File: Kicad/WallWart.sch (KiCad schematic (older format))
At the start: 7 parts, among them CON1 LB_BarrelJack, P2 V+_WallWart, U5 LM7805

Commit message: Layout with traces - ran through ERC and DRC
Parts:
- removed U5: LM7805, ~, symbol MCP1703
- added U3: MC78L05, ~, symbol MC78L05
- P2: value V+_WallWart -> WallWartExtension
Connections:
- net labels removed: Vin
- wire segments 15 -> 17
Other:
- moved on the sheet: P2
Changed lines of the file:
@@
 Sheet 4 7
 Title ""
-Date "14 aug 2014"
+Date "19 aug 2014"
 Rev ""
 Comp ""
@@
 Comment4 ""
 $EndDescr
-$Comp
-L MCP1703 U5
-U 1 1 53DB8BFE
-P 5600 3650
-F 0 "U5" H 5750 3650 60  0000 C CNN
-F 1 "LM7805" H 5600 4100 60  0000 C CNN
-F 2 "~" H 5600 3650 60  0000 C CNN
-F 3 "~" H 5600 3650 60  0000 C CNN
-	1    5600 3650
-	1    0    0    -1
-$EndComp
 $Comp
 L C C12
@@
 $EndComp
 Wire Wire Line
-	6250 3450 7950 3450
-Wire Wire Line
-	7200 3450 7200 3550
-Wire Wire Line
-	6800 3550 6800 3450
-Connection ~ 6800 3450
-Wire Wire Line
-	5600 3900 5600 4100
+	5600 3750 5600 4100
 Wire Wire Line
 	3750 4100 7200 4100
@@
 	6800 3950 6800 4100
 Connection ~ 6800 4100
-Wire Wire Line
-	4350 3450 5000 3450
-Wire Wire Line
-	4750 3450 4750 3550
 Wire Wire Line
 	4750 4100 4750 3950
@@
 Wire Wire Line
 	3950 3450 3750 3450
-Connection ~ 4750 3450
 Wire Wire Line
 	3750 3550 3750 4100
 Connection ~ 4750 4100
 Connection ~ 3750 3650
-Connection ~ 7200 3450
 Text Notes 3150 3150 0    60   ~ 0
 6.25V - 12V
@@
 V+_WallWart
 $Comp
-L AGND #PWR10
+L AGND #PWR010
 U 1 1 53DCDB22
 P 5250 4450
-F 0 "#PWR10" H 5250 4450 40  0001 C CNN
+F 0 "#PWR010" H 5250 4450 40  0001 C CNN
 F 1 "AGND" H 5250 4380 50  0000 C CNN
 F 2 "" H 5250 4450 60  0000 C CNN
@@
 	5250 4450 5250 4100
 Connection ~ 5250 4100
-Text Label 4850 3450 0    60   ~ 0
-Vin
-Text Label 3850 3450 0    60   ~ 0
-Vin
 $Comp
 L CONN_2 P2
 U 1 1 53E89338
-P 7500 2900
-F 0 "P2" V 7450 2900 40  0000 C CNN
-F 1 "V+_WallWart" V 7550 2900 40  0000 C CNN
-F 2 "" H 7500 2900 60  0000 C CNN
-F 3 "" H 7500 2900 60  0000 C CNN
-	1    7500 2900
+P 7500 2450
+F 0 "P2" V 7450 2450 40  0000 C CNN
+F 1 "WallWartExtension" V 7550 2450 40  0000 C CNN
+F 2 "" H 7500 2450 60  0000 C CNN
+F 3 "" H 7500 2450 60  0000 C CNN
+	1    7500 2450
 	0    -1   -1   0
 $EndComp
 Wire Wire Line
-	7400 3250 7400 3450
-Connection ~ 7400 3450
+	7600 2800 7600 3450
+$Comp
+L AGND #PWR011
+U 1 1 53F2345C
+P 7400 2950
+F 0 "#PWR011" H 7400 2950 40  0001 C CNN
+F 1 "AGND" H 7400 2880 50  0000 C CNN
+F 2 "" H 7400 2950 60  0000 C CNN
+F 3 "" H 7400 2950 60  0000 C CNN
+	1    7400 2950
+	1    0    0    -1
+$EndComp
 Wire Wire Line
-	7600 3250 7600 3450
-Connection ~ 7600 3450
+	7400 2800 7400 2950
+$Comp
+L MC78L05 U3
+U 1 1 53F37E5C
+P 5600 3500
+F 0 "U3" H 5750 3500 60  0000 C CNN
+F 1 "MC78L05" H 5600 3950 60  0000 C CNN
+F 2 "~" H 5600 3500 60  0000 C CNN
+F 3 "~" H 5600 3500 60  0000 C CNN
+	1    5600 3500
+	1    0    0    -1
+$EndComp
+Wire Wire Line
+	6250 3300 7200 3300
+Wire Wire Line
+	7200 3300 7200 3550
+Wire Wire Line
+	6800 3550 6800 3300
+Connection ~ 6800 3300
+Wire Wire Line
+	4350 3450 4450 3450
+Wire Wire Line
+	4450 3450 4450 3300
+Wire Wire Line
+	4450 3300 5000 3300
+Wire Wire Line
+	4750 3550 4750 3300
+Connection ~ 4750 3300
 $EndSCHEMATC

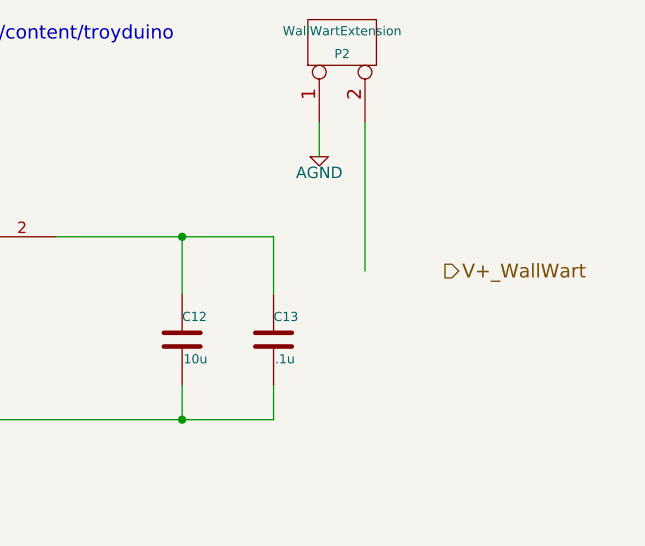
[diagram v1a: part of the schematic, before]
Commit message: updates to layout based on DRC/DFM checks
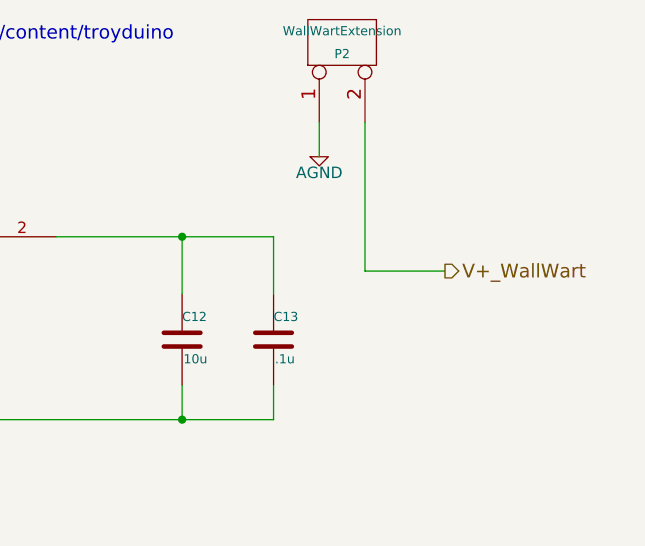
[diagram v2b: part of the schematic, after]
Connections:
- wire segments 17 -> 18
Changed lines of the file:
@@
 Sheet 4 7
 Title ""
-Date "19 aug 2014"
+Date "20 aug 2014"
 Rev ""
 Comp ""
@@
 	4750 3550 4750 3300
 Connection ~ 4750 3300
+Wire Wire Line
+	7600 3450 7950 3450
 $EndSCHEMATC

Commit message: Dev Rev 1
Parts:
- added D3: 4004, ~, symbol DIODE
- added TP10, TP11, TP9: CONN_1, symbol CONN_1
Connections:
- net AGND: now also TP10.1
- net V+_WallWart: now also D3.2 (K), TP11.1; no longer P2.2 (PM)
- net at C12.1, C13.1, U3.2: now also P2.2 (PM), D3.1 (A)
- net at C11.1, D2.2 (K), U3.3: now also TP9.1
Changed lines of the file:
@@
 Sheet 4 7
 Title ""
-Date "20 aug 2014"
+Date "21 aug 2014"
 Rev ""
 Comp ""
@@
 Text Notes 4700 2450 0    60   ~ 0
 see http://www.troydowling.org/content/troyduino
-Text HLabel 7950 3450 2    60   Output ~ 0
+Text HLabel 9150 3450 2    60   Output ~ 0
 V+_WallWart
 $Comp
@@
 $EndComp
 Wire Wire Line
-	6250 3300 7200 3300
+	6250 3300 7600 3300
 Wire Wire Line
 	7200 3300 7200 3550
@@
 Connection ~ 6800 3300
 Wire Wire Line
-	4350 3450 4450 3450
-Wire Wire Line
-	4450 3450 4450 3300
+	4450 3450 4350 3450
+Wire Wire Line
+	4450 3050 4450 3450
 Wire Wire Line
 	4450 3300 5000 3300
@@
 Connection ~ 4750 3300
 Wire Wire Line
-	7600 3450 7950 3450
+	7600 3450 8350 3450
+Connection ~ 7200 3300
+Connection ~ 7600 3300
+$Comp
+L DIODE D3
+U 1 1 53F5B6B0
+P 8550 3450
+F 0 "D3" H 8550 3550 40  0000 C CNN
+F 1 "4004" H 8550 3350 40  0000 C CNN
+F 2 "~" H 8550 3450 60  0000 C CNN
+F 3 "~" H 8550 3450 60  0000 C CNN
+	1    8550 3450
+	1    0    0    -1
+$EndComp
+Wire Wire Line
+	8750 3450 9150 3450
+$Comp
+L CONN_1 TP9
+U 1 1 53F5FBA0
+P 4600 3050
+F 0 "TP9" H 4680 3050 40  0000 L CNN
+F 1 "CONN_1" H 4600 3105 30  0001 C CNN
+F 2 "" H 4600 3050 60  0000 C CNN
+F 3 "" H 4600 3050 60  0000 C CNN
+	1    4600 3050
+	1    0    0    -1
+$EndComp
+Connection ~ 4450 3300
+$Comp
+L CONN_1 TP11
+U 1 1 53F5FBD1
+P 9100 3000
+F 0 "TP11" H 9180 3000 40  0000 L CNN
+F 1 "CONN_1" H 9100 3055 30  0001 C CNN
+F 2 "" H 9100 3000 60  0000 C CNN
+F 3 "" H 9100 3000 60  0000 C CNN
+	1    9100 3000
+	1    0    0    -1
+$EndComp
+Wire Wire Line
+	8950 3000 8950 3450
+Connection ~ 8950 3450
+$Comp
+L CONN_1 TP10
+U 1 1 53F5FBF5
+P 6250 3850
+F 0 "TP10" H 6330 3850 40  0000 L CNN
+F 1 "CONN_1" H 6250 3905 30  0001 C CNN
+F 2 "" H 6250 3850 60  0000 C CNN
+F 3 "" H 6250 3850 60  0000 C CNN
+	1    6250 3850
+	1    0    0    -1
+$EndComp
+Wire Wire Line
+	6100 3850 6100 4100
+Connection ~ 6100 4100
 $EndSCHEMATC

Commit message: updates for dev rev 2
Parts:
- removed TP11: CONN_1, symbol CONN_1
- added D?: LED, ~, symbol LED
- added R?: 120, ~, symbol R
- added TP?: CONN_1, symbol CONN_1
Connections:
- net V+_WallWart: now also D?.2 (K), TP?.1; no longer D3.2 (K)
- net at C12.1, C13.1, D3.1 (A)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: no longer P2.2 (PM)
- new net: D3.2 (K), P2.2 (PM), R?.1
- new net: D?.1 (A), R?.2
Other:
- moved on the sheet: D3, P2
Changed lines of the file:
@@
 Sheet 4 7
 Title ""
-Date "21 aug 2014"
+Date "9 sep 2014"
 Rev ""
 Comp ""
@@
 $EndComp
 Wire Wire Line
-	5600 3750 5600 4100
+	5600 4100 5600 3750
 Wire Wire Line
 	3750 4100 7200 4100
@@
 Text Notes 4700 2450 0    60   ~ 0
 see http://www.troydowling.org/content/troyduino
-Text HLabel 9150 3450 2    60   Output ~ 0
+Text HLabel 10050 3300 2    60   Output ~ 0
 V+_WallWart
 $Comp
@@
 L CONN_2 P2
 U 1 1 53E89338
-P 7500 2450
-F 0 "P2" V 7450 2450 40  0000 C CNN
-F 1 "WallWartExtension" V 7550 2450 40  0000 C CNN
-F 2 "" H 7500 2450 60  0000 C CNN
-F 3 "" H 7500 2450 60  0000 C CNN
-	1    7500 2450
+P 8250 2450
+F 0 "P2" V 8200 2450 40  0000 C CNN
+F 1 "WallWartExtension" V 8300 2450 40  0000 C CNN
+F 2 "" H 8250 2450 60  0000 C CNN
+F 3 "" H 8250 2450 60  0000 C CNN
+	1    8250 2450
 	0    -1   -1   0
 $EndComp
 Wire Wire Line
-	7600 2800 7600 3450
+	8350 2800 8350 3300
 $Comp
 L AGND #PWR011
 U 1 1 53F2345C
-P 7400 2950
-F 0 "#PWR011" H 7400 2950 40  0001 C CNN
-F 1 "AGND" H 7400 2880 50  0000 C CNN
-F 2 "" H 7400 2950 60  0000 C CNN
-F 3 "" H 7400 2950 60  0000 C CNN
-	1    7400 2950
-	1    0    0    -1
-$EndComp
-Wire Wire Line
-	7400 2800 7400 2950
+P 8150 2950
+F 0 "#PWR011" H 8150 2950 40  0001 C CNN
+F 1 "AGND" H 8150 2880 50  0000 C CNN
+F 2 "" H 8150 2950 60  0000 C CNN
+F 3 "" H 8150 2950 60  0000 C CNN
+	1    8150 2950
+	1    0    0    -1
+$EndComp
+Wire Wire Line
+	8150 2800 8150 2950
 $Comp
 L MC78L05 U3
@@
 $EndComp
 Wire Wire Line
-	6250 3300 7600 3300
-Wire Wire Line
-	7200 3300 7200 3550
-Wire Wire Line
-	6800 3550 6800 3300
+	6250 3300 7400 3300
+Wire Wire Line
+	6800 3300 6800 3550
 Connection ~ 6800 3300
 Wire Wire Line
@@
 	4750 3550 4750 3300
 Connection ~ 4750 3300
-Wire Wire Line
-	7600 3450 8350 3450
-Connection ~ 7200 3300
-Connection ~ 7600 3300
+Connection ~ 8350 3300
 $Comp
 L DIODE D3
 U 1 1 53F5B6B0
-P 8550 3450
-F 0 "D3" H 8550 3550 40  0000 C CNN
-F 1 "4004" H 8550 3350 40  0000 C CNN
-F 2 "~" H 8550 3450 60  0000 C CNN
-F 3 "~" H 8550 3450 60  0000 C CNN
-	1    8550 3450
-	1    0    0    -1
-$EndComp
-Wire Wire Line
-	8750 3450 9150 3450
+P 7600 3300
+F 0 "D3" H 7600 3400 40  0000 C CNN
+F 1 "4004" H 7600 3200 40  0000 C CNN
+F 2 "~" H 7600 3300 60  0000 C CNN
+F 3 "~" H 7600 3300 60  0000 C CNN
+	1    7600 3300
+	1    0    0    -1
+$EndComp
 $Comp
 L CONN_1 TP9
@@
 Connection ~ 4450 3300
 $Comp
-L CONN_1 TP11
-U 1 1 53F5FBD1
-P 9100 3000
-F 0 "TP11" H 9180 3000 40  0000 L CNN
-F 1 "CONN_1" H 9100 3055 30  0001 C CNN
-F 2 "" H 9100 3000 60  0000 C CNN
-F 3 "" H 9100 3000 60  0000 C CNN
-	1    9100 3000
-	1    0    0    -1
-$EndComp
-Wire Wire Line
-	8950 3000 8950 3450
-Connection ~ 8950 3450
-$Comp
 L CONN_1 TP10
 U 1 1 53F5FBF5
@@
 	6100 3850 6100 4100
 Connection ~ 6100 4100
+$Comp
+L LED D?
+U 1 1 540ED65C
+P 9400 3300
+F 0 "D?" H 9400 3400 50  0000 C CNN
+F 1 "LED" H 9400 3200 50  0000 C CNN
+F 2 "~" H 9400 3300 60  0000 C CNN
+F 3 "~" H 9400 3300 60  0000 C CNN
+	1    9400 3300
+	1    0    0    -1
+$EndComp
+Text Label 8100 3700 0    60   ~ 0
+Green Status LED always on when there is power
+$Comp
+L R R?
+U 1 1 540EDC27
+P 8750 3300
+F 0 "R?" V 8830 3300 40  0000 C CNN
+F 1 "120" V 8757 3301 40  0000 C CNN
+F 2 "~" V 8680 3300 30  0000 C CNN
+F 3 "~" H 8750 3300 30  0000 C CNN
+	1    8750 3300
+	0    -1   -1   0
+$EndComp
+Wire Wire Line
+	7800 3300 8500 3300
+Wire Wire Line
+	9000 3300 9200 3300
+Wire Wire Line
+	9600 3300 10050 3300
+Wire Wire Line
+	7200 3300 7200 3550
+Connection ~ 7200 3300
+Text Label 7050 1600 0    60   ~ 0
+http://media.digikey.com/pdf/Data%20Sheets/Lite-On%20PDFs/LTST-C171GKT.pdf
+Text Label 8600 1300 0    60   ~ 0
+LED: 20mA, 2.5 forward voltage
+$Comp
+L CONN_1 TP?
+U 1 1 540EE2E1
+P 9950 2950
+F 0 "TP?" H 10030 2950 40  0000 L CNN
+F 1 "CONN_1" H 9950 3005 30  0001 C CNN
+F 2 "" H 9950 2950 60  0000 C CNN
+F 3 "" H 9950 2950 60  0000 C CNN
+	1    9950 2950
+	1    0    0    -1
+$EndComp
+Wire Wire Line
+	9800 2950 9800 3300
+Connection ~ 9800 3300
 $EndSCHEMATC

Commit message: Ready for Schematic Design Review
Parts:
- removed D3: 4004, ~, symbol DIODE
- R5: renamed from R?; value 120 -> 1K
- gave numbers to parts that had none: 2
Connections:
- net AGND: now also R5.1
- net V+_WallWart: now also C12.1, C13.1, D3.1 (A), P2.2 (PM), U3.2; no longer D3.2 (K)
- net at R5.2: now also D3.2 (K); no longer D3.1 (A)
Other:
- note removed: "see http://www.troydowling.org/content/troyduino"
- moved on the sheet: D3, R5
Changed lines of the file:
@@
 $Descr A4 11693 8268
 encoding utf-8
-Sheet 4 7
+Sheet 2 7
 Title ""
-Date "9 sep 2014"
+Date "10 sep 2014"
 Rev ""
 Comp ""
@@
 Text Notes 3150 3150 0    60   ~ 0
 6.25V - 12V
-Text Notes 4700 2450 0    60   ~ 0
-see http://www.troydowling.org/content/troyduino
 Text HLabel 10050 3300 2    60   Output ~ 0
 V+_WallWart
 $Comp
-L AGND #PWR010
+L AGND #PWR01
 U 1 1 53DCDB22
 P 5250 4450
-F 0 "#PWR010" H 5250 4450 40  0001 C CNN
+F 0 "#PWR01" H 5250 4450 40  0001 C CNN
 F 1 "AGND" H 5250 4380 50  0000 C CNN
 F 2 "" H 5250 4450 60  0000 C CNN
@@
 $EndComp
 Wire Wire Line
-	8350 2800 8350 3300
-$Comp
-L AGND #PWR011
+	8350 3300 8350 2800
+$Comp
+L AGND #PWR02
 U 1 1 53F2345C
 P 8150 2950
-F 0 "#PWR011" H 8150 2950 40  0001 C CNN
+F 0 "#PWR02" H 8150 2950 40  0001 C CNN
 F 1 "AGND" H 8150 2880 50  0000 C CNN
 F 2 "" H 8150 2950 60  0000 C CNN
@@
 $EndComp
 Wire Wire Line
-	6250 3300 7400 3300
-Wire Wire Line
 	6800 3300 6800 3550
-Connection ~ 6800 3300
 Wire Wire Line
 	4450 3450 4350 3450
@@
 	4750 3550 4750 3300
 Connection ~ 4750 3300
-Connection ~ 8350 3300
-$Comp
-L DIODE D3
-U 1 1 53F5B6B0
-P 7600 3300
-F 0 "D3" H 7600 3400 40  0000 C CNN
-F 1 "4004" H 7600 3200 40  0000 C CNN
-F 2 "~" H 7600 3300 60  0000 C CNN
-F 3 "~" H 7600 3300 60  0000 C CNN
-	1    7600 3300
-	1    0    0    -1
-$EndComp
 $Comp
 L CONN_1 TP9
@@
 Connection ~ 6100 4100
 $Comp
-L LED D?
+L LED D3
 U 1 1 540ED65C
-P 9400 3300
-F 0 "D?" H 9400 3400 50  0000 C CNN
-F 1 "LED" H 9400 3200 50  0000 C CNN
-F 2 "~" H 9400 3300 60  0000 C CNN
-F 3 "~" H 9400 3300 60  0000 C CNN
-	1    9400 3300
-	1    0    0    -1
-$EndComp
-Text Label 8100 3700 0    60   ~ 0
-Green Status LED always on when there is power
-$Comp
-L R R?
+P 8850 3700
+F 0 "D3" H 8850 3800 50  0000 C CNN
+F 1 "LED" H 8850 3600 50  0000 C CNN
+F 2 "~" H 8850 3700 60  0000 C CNN
+F 3 "~" H 8850 3700 60  0000 C CNN
+	1    8850 3700
+	0    1    1    0
+$EndComp
+$Comp
+L R R5
 U 1 1 540EDC27
-P 8750 3300
-F 0 "R?" V 8830 3300 40  0000 C CNN
-F 1 "120" V 8757 3301 40  0000 C CNN
-F 2 "~" V 8680 3300 30  0000 C CNN
-F 3 "~" H 8750 3300 30  0000 C CNN
-	1    8750 3300
-	0    -1   -1   0
-$EndComp
-Wire Wire Line
-	7800 3300 8500 3300
-Wire Wire Line
-	9000 3300 9200 3300
-Wire Wire Line
-	9600 3300 10050 3300
+P 8850 4400
+F 0 "R5" V 8930 4400 40  0000 C CNN
+F 1 "1K" V 8857 4401 40  0000 C CNN
+F 2 "~" V 8780 4400 30  0000 C CNN
+F 3 "~" H 8850 4400 30  0000 C CNN
+	1    8850 4400
+	-1   0    0    1
+$EndComp
+Wire Wire Line
+	6250 3300 10050 3300
 Wire Wire Line
 	7200 3300 7200 3550
-Connection ~ 7200 3300
-Text Label 7050 1600 0    60   ~ 0
-http://media.digikey.com/pdf/Data%20Sheets/Lite-On%20PDFs/LTST-C171GKT.pdf
-Text Label 8600 1300 0    60   ~ 0
-LED: 20mA, 2.5 forward voltage
-$Comp
-L CONN_1 TP?
+$Comp
+L CONN_1 TP8
 U 1 1 540EE2E1
 P 9950 2950
-F 0 "TP?" H 10030 2950 40  0000 L CNN
+F 0 "TP8" H 10030 2950 40  0000 L CNN
 F 1 "CONN_1" H 9950 3005 30  0001 C CNN
 F 2 "" H 9950 2950 60  0000 C CNN
@@
 	9800 2950 9800 3300
 Connection ~ 9800 3300
+Connection ~ 6800 3300
+Connection ~ 7200 3300
+Connection ~ 8350 3300
+Wire Wire Line
+	8850 3500 8850 3300
+Connection ~ 8850 3300
+Wire Wire Line
+	8850 3900 8850 4150
+Wire Wire Line
+	8850 4650 8850 4900
+$Comp
+L AGND #PWR03
+U 1 1 5410156B
+P 8850 4900
+F 0 "#PWR03" H 8850 4900 40  0001 C CNN
+F 1 "AGND" H 8850 4830 50  0000 C CNN
+F 2 "" H 8850 4900 60  0000 C CNN
+F 3 "" H 8850 4900 60  0000 C CNN
+	1    8850 4900
+	1    0    0    -1
+$EndComp
 $EndSCHEMATC

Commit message: Layout ready for final check prior to PCB fab
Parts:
- added TP19, TP20: CONN_1, symbol CONN_1
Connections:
- net AGND: now also TP19.1
- net at CON1.1, D2.1 (A): now also TP20.1
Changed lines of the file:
@@
 Sheet 2 7
 Title ""
-Date "11 sep 2014"
+Date "13 sep 2014"
 Rev ""
 Comp ""
@@
 Connection ~ 4750 4100
 Connection ~ 3750 3650
-Text Notes 3150 3150 0    60   ~ 0
+Text Notes 2750 3150 0    60   ~ 0
 6.25V - 12V
 Text HLabel 10050 3300 2    60   Output ~ 0
@@
 	1    0    0    -1
 $EndComp
+$Comp
+L CONN_1 TP20
+U 1 1 54142B38
+P 4050 3100
+F 0 "TP20" H 4130 3100 40  0000 L CNN
+F 1 "CONN_1" H 4050 3155 30  0001 C CNN
+F 2 "" H 4050 3100 60  0000 C CNN
+F 3 "" H 4050 3100 60  0000 C CNN
+	1    4050 3100
+	1    0    0    -1
+$EndComp
+Wire Wire Line
+	3900 3100 3900 3450
+Connection ~ 3900 3450
+$Comp
+L CONN_1 TP19
+U 1 1 54142B64
+P 3300 4000
+F 0 "TP19" H 3380 4000 40  0000 L CNN
+F 1 "CONN_1" H 3300 4055 30  0001 C CNN
+F 2 "" H 3300 4000 60  0000 C CNN
+F 3 "" H 3300 4000 60  0000 C CNN
+	1    3300 4000
+	-1   0    0    1
+$EndComp
+Wire Wire Line
+	3450 4000 3750 4000
+Connection ~ 3750 4000
 $EndSCHEMATC
